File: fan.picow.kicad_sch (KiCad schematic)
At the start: 44 parts, among them Q1 BSS138, Q2 BSS138, Q3 IRLML9301TRPBF, SW1 EG1257, U1 PicoW

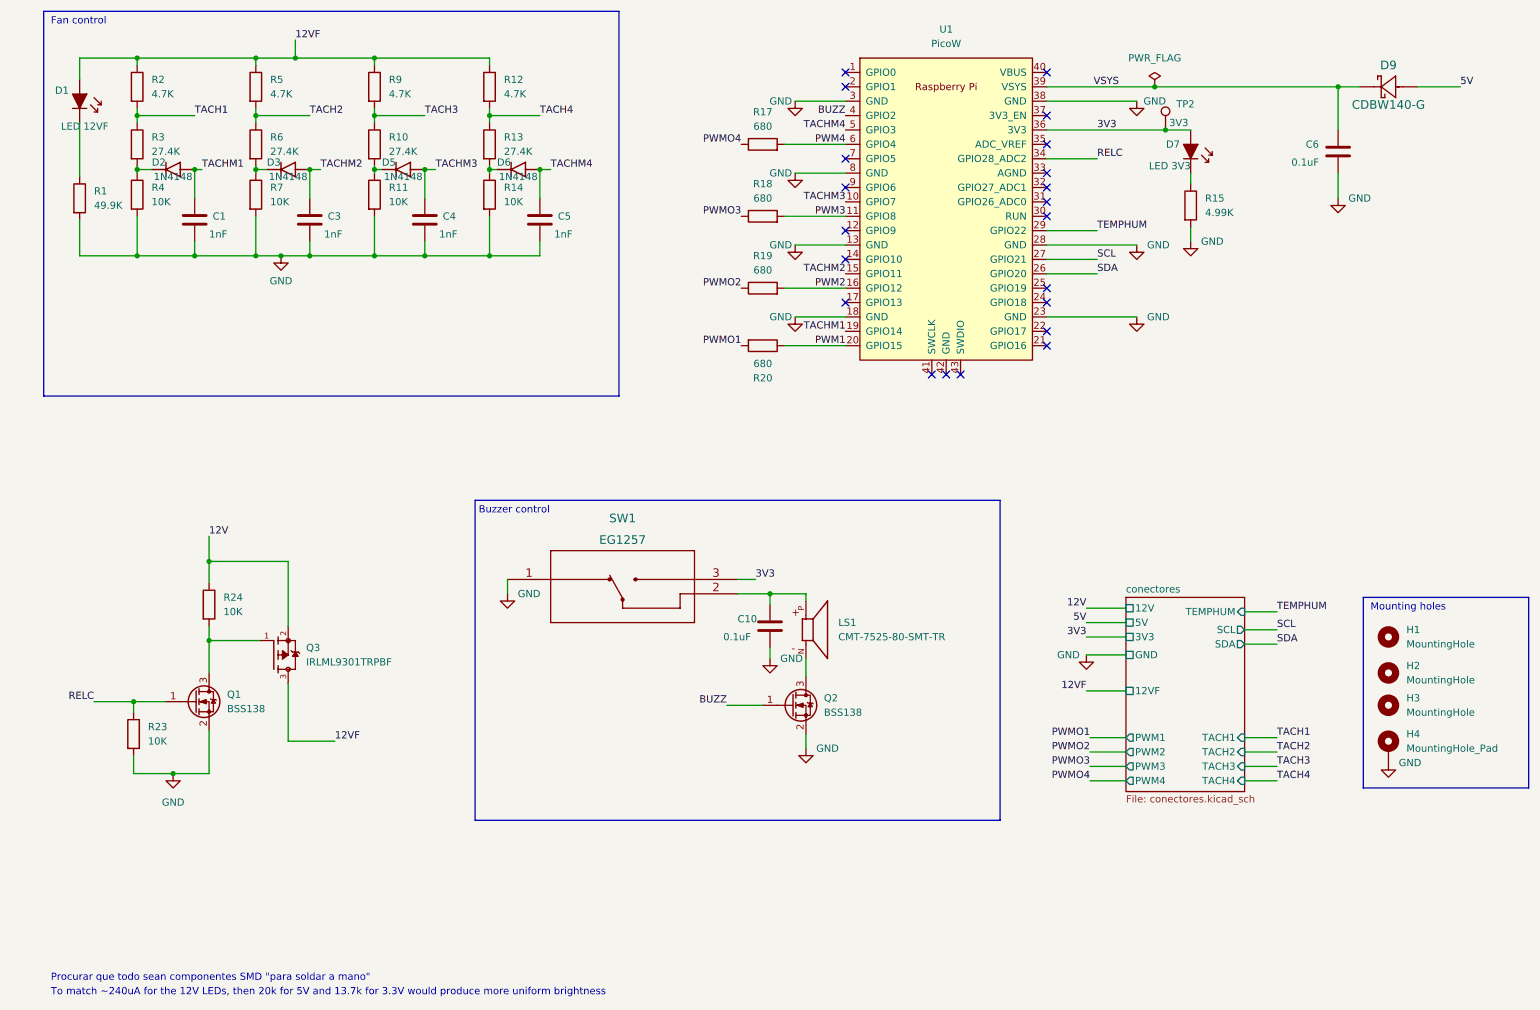
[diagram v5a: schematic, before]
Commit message: edit some footprints to give more room to the pads
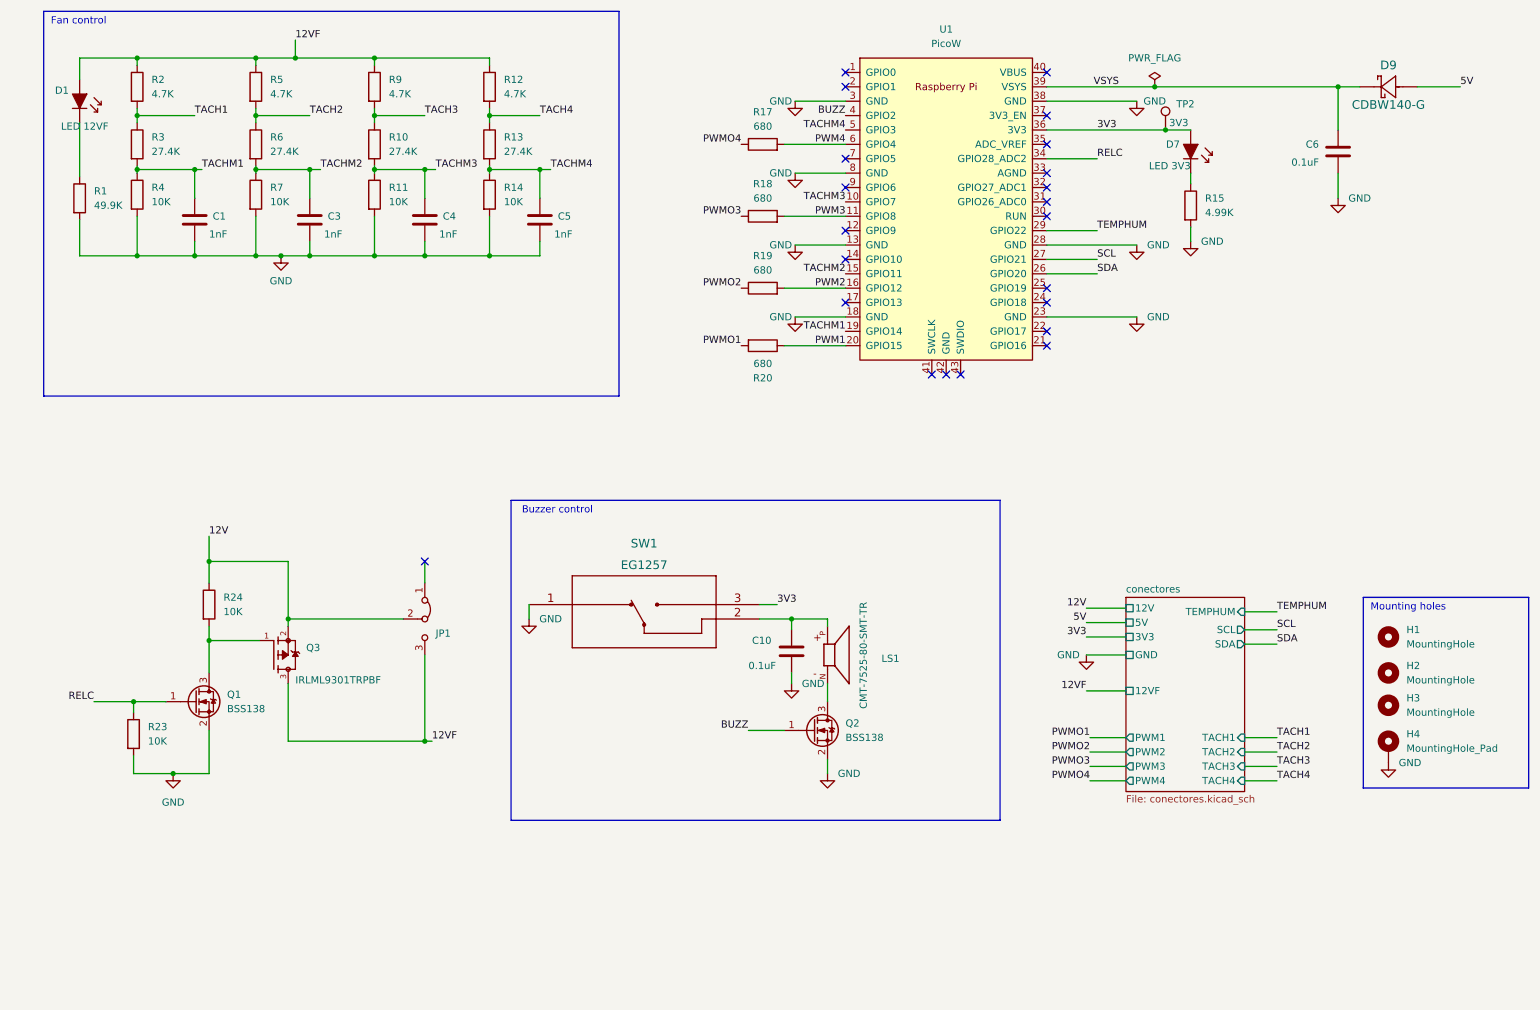
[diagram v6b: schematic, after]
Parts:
- removed D2, D3, D5, D6: 1N4148, Diode_SMD:D_SOD-123, symbol 1N4148W:1N4148W
- added JP1: Jumper_3_Bridged12, Connector_PinHeader_2.54mm:PinHeader_1x03_P2.54mm_Vertical, symbol Jumper:Jumper_3_Bridged12
- C1, C10, C3, C4, C5, C6: footprint Capacitor_SMD:C_0603_1608Metric_Pad1.08x0.95mm_HandSolder -> Capacitor_SMD:C_0805_2012Metric_Pad1.18x1.45mm_HandSolder
- R1, R10, R11, R12, R13, R14, R15, R17, R18, R19, R2, R20, R23, R24, R3, R4, R5, R6, R7, R9: footprint Resistor_SMD:R_0603_1608Metric_Pad0.98x0.95mm_HandSolder -> Resistor_SMD:R_0805_2012Metric_Pad1.20x1.40mm_HandSolder
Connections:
- net 12V: now also JP1.2 (C)
- net 12VF: now also JP1.3 (B)
- net TACHM1: now also R3.2, R4.1
- net TACHM2: now also R6.2, R7.1
- net TACHM3: now also R10.2, R11.1
- net TACHM4: now also R13.2, R14.1
- no-connect marks 21 -> 22
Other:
- note removed: "Procurar que todo sean componentes SMD "para soldar a mano""
- note removed: "To match ~240uA for the 12V LEDs, then 20k for 5V and 13.7k for 3.3V would produce more uniform brightness"
- moved on the sheet: C10, LS1, Q2, SW1

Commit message: synch sch and pcb
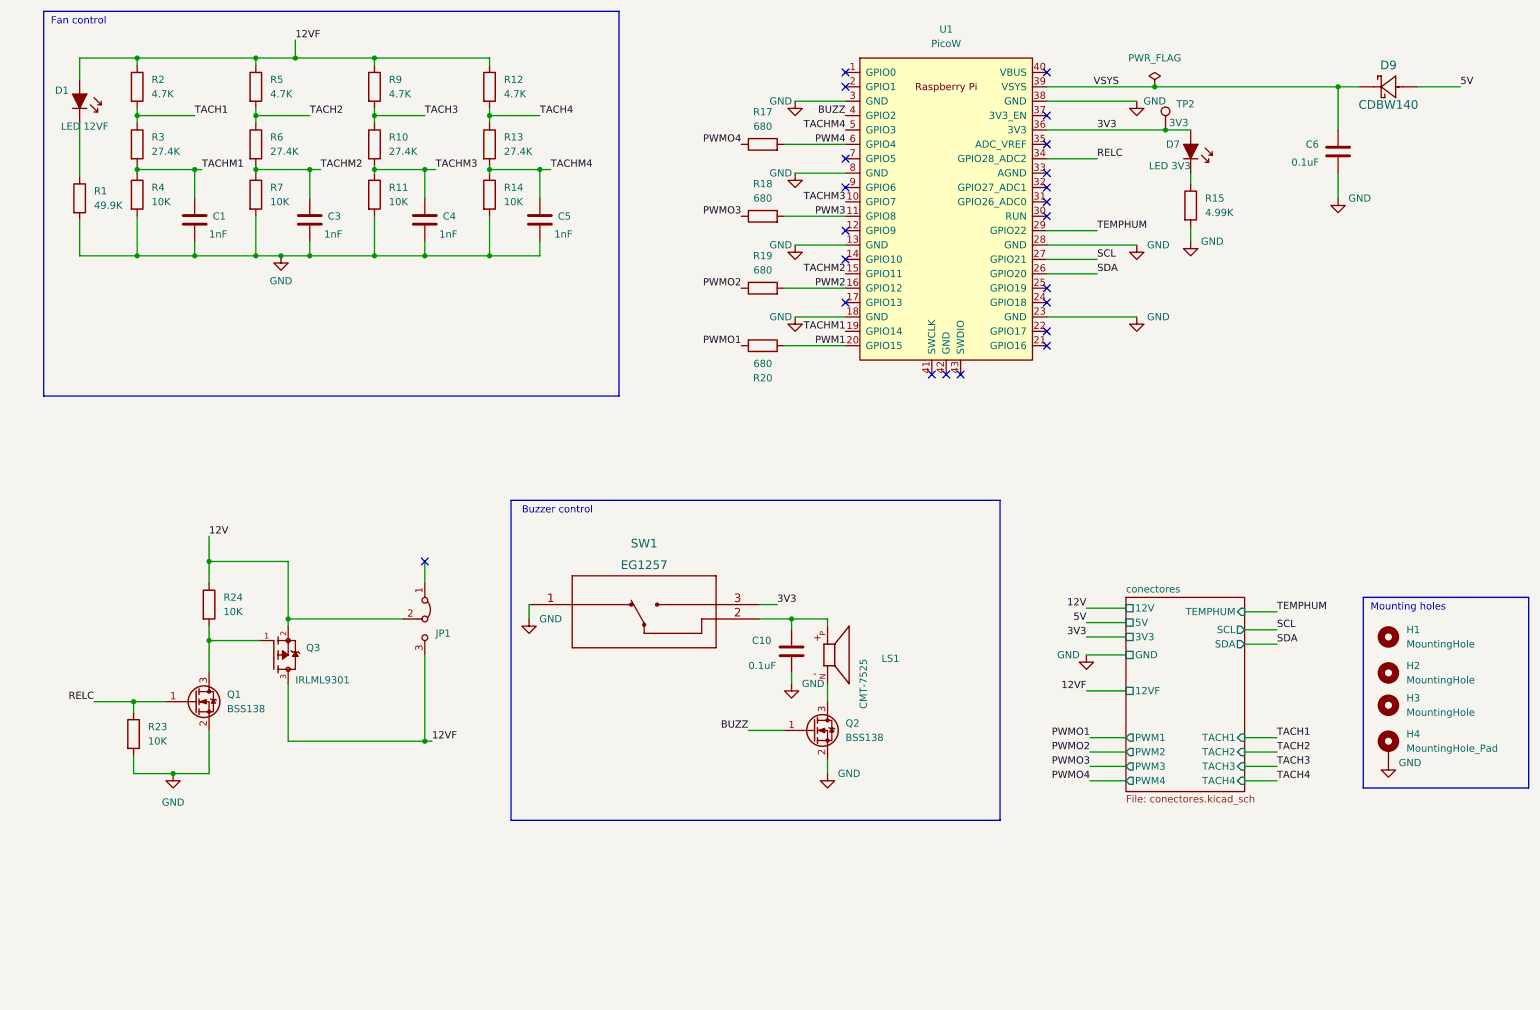
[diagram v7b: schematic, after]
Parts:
- D9: value CDBW140-G -> CDBW140
- LS1: value CMT-7525-80-SMT-TR -> CMT-7525; Componente (none) -> CMT-7525-80-SMT-TR
- Q3: value IRLML9301TRPBF -> IRLML9301
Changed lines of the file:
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@@
       (effects (font (size 1.27 1.27)) (justify left))
     )
-    (property "Value" "IRLML9301TRPBF" (id 1) (at 62.865 137.795 0)
+    (property "Value" "IRLML9301" (id 1) (at 62.865 137.795 0)
       (effects (font (size 1.27 1.27)) (justify left))
     )
@@
       (effects (font (size 1.27 1.27)) (justify left))
     )
-    (property "Value" "CMT-7525-80-SMT-TR" (id 1) (at 163.195 142.875 90)
+    (property "Value" "CMT-7525" (id 1) (at 163.195 142.875 90)
       (effects (font (size 1.27 1.27)) (justify left))
     )
@@
     (property "MAXIMUM_PACKAGE_HEIGHT" "2.50mm" (id 7) (at 156.845 133.35 0)
       (effects (font (size 1.27 1.27)) (justify bottom) hide)
+    )
+    (property "Componente" "CMT-7525-80-SMT-TR" (id 8) (at 156.845 133.35 0)
+      (effects (font (size 1.27 1.27)) hide)
     )
     (pin "N")
@@
       (effects (font (size 1.524 1.524)))
     )
-    (property "Value" "CDBW140-G" (id 1) (at 255.905 36.195 0)
+    (property "Value" "CDBW140" (id 1) (at 255.905 36.195 0)
       (effects (font (size 1.524 1.524)))
     )
@@
     )
     (path "/86e12817-80ac-414c-aa23-eca04293b568/8d5ca4e5-a782-47d9-9971-0676e6a8b021"
-      (reference "D2") (unit 1) (value "CDBW140-G") (footprint "Diode_SMD:D_SOD-123F")
+      (reference "D2") (unit 1) (value "CDBW140") (footprint "Diode_SMD:D_SOD-123F")
     )
     (path "/86e12817-80ac-414c-aa23-eca04293b568/bf20e1da-f16a-481e-8566-f9b46e75b06d"
@@
     )
     (path "/fcc4f7b1-a256-4edb-9e34-1c38fb03135b"
-      (reference "D9") (unit 1) (value "CDBW140-G") (footprint "Diode_SMD:D_SOD-123F")
+      (reference "D9") (unit 1) (value "CDBW140") (footprint "Diode_SMD:D_SOD-123F")
     )
     (path "/86e12817-80ac-414c-aa23-eca04293b568/5122c57c-28dc-41b6-be93-119eb3e6ad19"
@@
     )
     (path "/86e12817-80ac-414c-aa23-eca04293b568/d7641a10-1696-479f-8ad9-c72747f4c20a"
-      (reference "J1") (unit 1) (value "12v Input") (footprint "Connector_PinHeader_2.54mm:PinHeader_1x02_P2.54mm_Vertical")
+      (reference "J1") (unit 1) (value "12v Input") (footprint "Connector_PinHeader_2.54mm:PinHeader_1x02_P2.54mm_Horizontal")
     )
     (path "/86e12817-80ac-414c-aa23-eca04293b568/1790f650-74c6-4ab3-b8d8-2a95be562786"
@@
     )
     (path "/86e12817-80ac-414c-aa23-eca04293b568/8b6c6ee4-7500-4b7b-b294-9ce1b523ab35"
-      (reference "J7") (unit 1) (value "OLED") (footprint "Connector_PinHeader_2.54mm:PinHeader_1x04_P2.54mm_Vertical")
+      (reference "J7") (unit 1) (value "OLED") (footprint "Connector_PinHeader_2.54mm:PinHeader_1x04_P2.54mm_Horizontal")
     )
     (path "/86e12817-80ac-414c-aa23-eca04293b568/bdd943df-b6d2-4f3d-b75e-b8fb7a4fe4f2"
-      (reference "J12") (unit 1) (value "Temp DHT22") (footprint "Connector_PinHeader_2.54mm:PinHeader_1x03_P2.54mm_Vertical")
+      (reference "J12") (unit 1) (value "Temp") (footprint "Connector_PinHeader_2.54mm:PinHeader_1x03_P2.54mm_Horizontal")
     )
     (path "/3c7d9133-dd36-448d-b86a-9f077007464b"
@@
     )
     (path "/3fe79dfd-60d0-4881-a73e-44d6645bbde6"
-      (reference "LS1") (unit 1) (value "CMT-7525-80-SMT-TR") (footprint "footprints descargados:XDCR_CMT-7525-80-SMT-TR")
+      (reference "LS1") (unit 1) (value "CMT-7525") (footprint "footprints descargados:XDCR_CMT-7525-80-SMT-TR")
     )
     (path "/24494c09-85e2-4bd7-849b-21573dc74f02"
@@
     )
     (path "/096dc07c-95db-4ea9-b8b6-ac23b1984d17"
-      (reference "Q3") (unit 1) (value "IRLML9301TRPBF") (footprint "footprints descargados:IRLML9301TRPBF.SOT95P237X112-3N")
+      (reference "Q3") (unit 1) (value "IRLML9301") (footprint "footprints descargados:IRLML9301TRPBF.SOT95P237X112-3N")
     )
     (path "/608007d4-b490-49e4-991d-4b210c673027"
@@
     )
     (path "/86e12817-80ac-414c-aa23-eca04293b568/8b0097ff-621f-47b0-bbc1-c49bbd9da7e6"
-      (reference "U3") (unit 1) (value "LM2575-5.0BU") (footprint "Package_TO_SOT_SMD:TO-263-5_TabPin3")
-    )
-  )
+      (reference "U3") (unit 1) (value "LM2575") (footprint "Package_TO_SOT_SMD:TO-263-5_TabPin3")
+    )
+  )

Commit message: Most SMD 1206 now
Also increase track size to 0.5 for Default subnet
And replace text so everything is more visible
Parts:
- C1, C10, C3, C4, C5, C6: footprint Capacitor_SMD:C_0805_2012Metric_Pad1.18x1.45mm_HandSolder -> Capacitor_SMD:C_1206_3216Metric_Pad1.33x1.80mm_HandSolder
- R1, R10, R11, R12, R13, R14, R15, R17, R18, R19, R2, R20, R23, R24, R3, R4, R5, R6, R7, R9: footprint Resistor_SMD:R_0805_2012Metric_Pad1.20x1.40mm_HandSolder -> Resistor_SMD:R_1206_3216Metric_Pad1.30x1.75mm_HandSolder
